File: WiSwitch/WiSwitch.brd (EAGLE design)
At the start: 58 x 58 mm, 22 parts, among them IC1 REG1117, T1 BT136

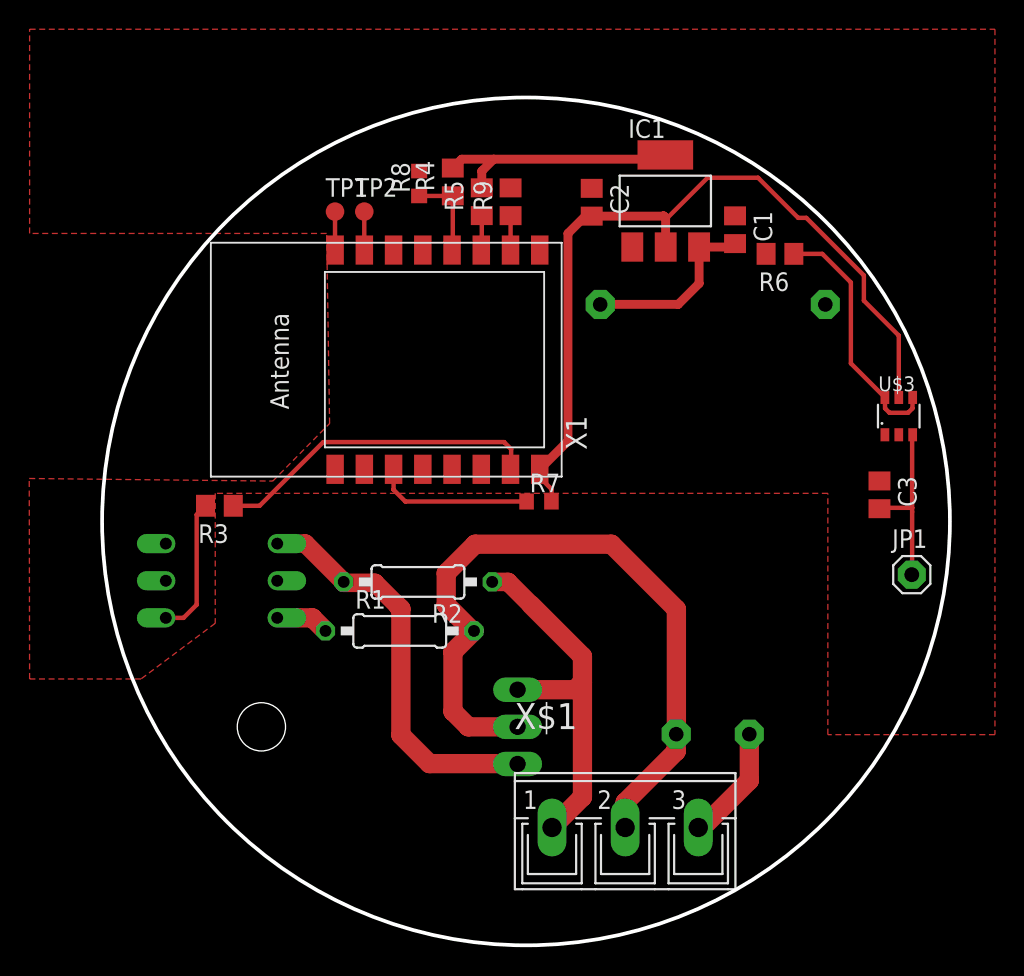
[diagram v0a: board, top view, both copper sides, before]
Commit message: updated WiSwitch, tiny433mhz and ade7953
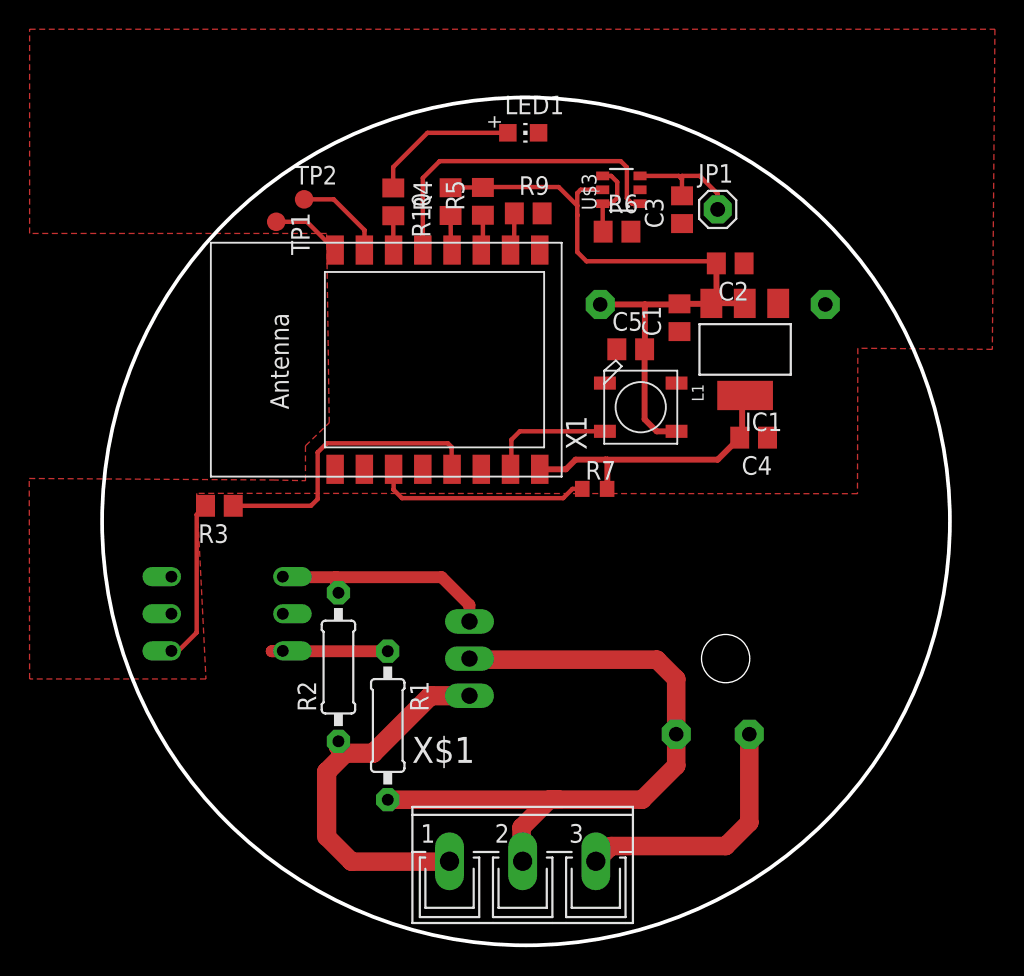
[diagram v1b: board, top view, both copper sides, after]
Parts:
- removed R8: (no value), rcl:R0603
- added C4, C5: (no value), rcl:C0805
- added L1: WS2812B, adafruit:WS2812B
- added LED1: (no value), adafruit:CHIP-LED0805
- added R10: 10k, rcl:R0805
- moved JP1 28.3 mm to (113.1, 141.3)
- moved U$3 24.5 mm to (106.5, 142.7), turned to 90 degrees
- moved C3 23.7 mm to (110.7, 141.3), turned to 90 degrees
- moved IC1 11.5 mm to (115.0, 131.8), turned to 180 degrees
- moved R6 11.2 mm to (106.2, 139.8), turned to 0 degrees
- moved T1 10.5 mm to (102.5, 110.6), turned to 90 degrees
- moved C2 10.4 mm to (114.0, 137.7), turned to 180 degrees
- moved R2 7.97 mm to (87.2, 110.0), turned to 90 degrees
- moved X$1 7.38 mm to (99.8, 96.7)
- moved C1 7.12 mm to (110.5, 133.9), turned to 90 degrees
- moved R1 6.52 mm to (90.5, 106.0), turned to 270 degrees
- moved TP2 4.20 mm to (84.8, 142.0)
- moved TP1 4.08 mm to (82.9, 140.5), turned to 270 degrees
- moved R7 3.91 mm to (104.7, 122.2)
- moved OK1 2.29 mm to (79.6, 113.7)
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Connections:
- net N$6 renamed TX
- net N$7 renamed RX
- new net GPIO4: R10.2, X1.14
- new net GPIO5: U$3.OUT, X1.13
- new net N$7: LED1.A, R10.1
- net 5V: now also C5.2, L1.1-VDD
- net GND: now also C4.1, C5.1, L1.3-GND, LED1.C; no longer R8.2
- net GPIO0: no longer R8.1
- net GPIO13: now also L1.4-DIN; no longer R3.1
- net GPIO14: now also R3.1, X1.5; no longer U$3.OUT
- net VCC: now also C4.2
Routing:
- net VCC: track 74.2 -> 49.4 mm
- net GPIO5: track 0.00 -> 22.7 mm
- net GPIO14: track 0.00 -> 20.2 mm
- net GPIO13: track 22.4 -> 8.69 mm
- net N$3: track 28.1 -> 15.8 mm
- net N$5: track 17.2 -> 5.37 mm
- net N$7: track 0.00 -> 10.2 mm
- net NEUTRAL: track 7.99 -> 17.6 mm
- net 5V: track 12.4 -> 18.0 mm
- net N$4: track 10.8 -> 14.8 mm
- net RX: track 2.63 -> 6.43 mm
- net IN: track 11.9 -> 8.34 mm
- net HOT: track 50.6 -> 47.0 mm
- net GPIO0: track 6.04 -> 2.52 mm
- net N$2: track 5.31 -> 8.70 mm
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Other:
- board text added: "WiSwitch 2016"
- board text removed: "N"
- board text removed: "OUT"
- board text removed: "~"
